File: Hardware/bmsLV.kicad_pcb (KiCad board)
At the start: 2 copper layers, 45 parts, among them J1 Conn_01x06_Male, J2 Conn_01x03_Female, J3 Conn_01x03_Female, J4 Conn_01x02_Female, J5 Conn_01x02_Female, SW1 SW_Push, U1 STM32F103C8Tx, U2 LM1117-3.3, U3 LM1117-3.3, U4 LM1117-3.3, U5 LM2596S-5, U6 MCP2562-H-SN, Y1 Crystal

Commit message: Going back to work
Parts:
- removed U5: LM2596S-5, Package_TO_SOT_SMD:TO-263-5_TabPin3
- removed U6: MCP2562-H-SN, Package_SO:SOIC-8_3.9x4.9mm_P1.27mm
- added C20: 10nF, Capacitor_SMD:C_1206_3216Metric, F.Cu at (210.8, 58.6)
- added C21: 10nF, Capacitor_SMD:C_1206_3216Metric, F.Cu at (173.5, 85.5)
- added C22: 10nF, Capacitor_SMD:C_1206_3216Metric, F.Cu at (202.5, 67.4)
- added C23: 10nF, Capacitor_SMD:C_1206_3216Metric, F.Cu at (217.2, 53.0)
- added C24: 10nF, Capacitor_SMD:C_1206_3216Metric, F.Cu at (185.0, 82.2)
- added C25: 1u, Capacitor_SMD:C_1206_3216Metric, F.Cu at (202.5, 64.1)
- added C26: 1u, Capacitor_SMD:C_1206_3216Metric, F.Cu at (179.1, 85.5)
- added C27: 1u, Capacitor_SMD:C_1206_3216Metric, F.Cu at (184.7, 85.5)
- added C28: 1u, Capacitor_SMD:C_1206_3216Metric, F.Cu at (179.4, 82.2)
- added C29: 0.1u, Capacitor_SMD:C_0603_1608Metric, F.Cu at (195.1, 87.2)
- added C30: 100n, Capacitor_SMD:C_1206_3216Metric, F.Cu at (253.8, 99.9)
- added C31: 100n, Capacitor_SMD:C_1206_3216Metric, F.Cu at (253.8, 96.6)
- added C32: 100n, Capacitor_SMD:C_1206_3216Metric, F.Cu at (236.0, 111.4)
- added C33: 100n, Capacitor_SMD:C_1206_3216Metric, F.Cu at (253.8, 93.3)
- added C34: 100n, Capacitor_SMD:C_1206_3216Metric, F.Cu at (230.4, 111.4)
- added C35: 100n, Capacitor_SMD:C_1206_3216Metric, F.Cu at (219.1, 111.4)
- added D10: 9.1V, Diode_SMD:D_SMB, F.Cu at (189.1, 72.2)
- added D11: 9.1V, Diode_SMD:D_SMB, F.Cu at (201.9, 54.1)
- added D12: 9.1V, Diode_SMD:D_SMB, F.Cu at (180.8, 77.8)
- added D13: 9.1V, Diode_SMD:D_SMB, F.Cu at (189.1, 77.8)
- added D14: 9.1V, Diode_SMD:D_SMB, F.Cu at (180.8, 72.2)
- added D15: 9.1V, Diode_SMD:D_SMB, F.Cu at (210.2, 54.1)
- added D16: D_Small, Diode_SMD:D_SMB, F.Cu at (130.4, 69.8)
- added D5: D_Schottky, Diode_SMD:D_SMB, F.Cu at (36.4, 109.9)
- added D6: D_Schottky, Diode_SMD:D_SMB, F.Cu at (78.3, 106.0)
- added D7: D_Schottky, Diode_SMD:D_SMB, F.Cu at (44.2, 114.9)
- added D8: D_TVS_x2_AAC, Package_TO_SOT_SMD:SOT-23, F.Cu at (159.3, 118.7)
- added D9: 9.1V, Diode_SMD:D_SMB, F.Cu at (203.9, 59.7)
- added FB1: Ferrite_Bead_Small, Capacitor_SMD:C_1206_3216Metric, F.Cu at (36.7, 106.0)
- added J10: Conn_01x01_Female, Connector_Pin:Pin_D1.0mm_L10.0mm_LooseFit, F.Cu at (48.2, 62.2)
- added J11: Conn_01x01_Female, Connector_Pin:Pin_D1.0mm_L10.0mm_LooseFit, F.Cu at (27.9, 62.2)
- added J12: Conn_01x01_Female, Connector_Pin:Pin_D1.0mm_L10.0mm_LooseFit, F.Cu at (28.1, 112.7)
- added J13: Conn_01x04_Male, Connector_PinHeader_2.54mm:PinHeader_1x04_P2.54mm_Vertical, F.Cu at (122.6, 109.9)
- added J6: Conn_01x01_Female, Connector_Pin:Pin_D1.0mm_L10.0mm_LooseFit, F.Cu at (129.1, 62.2)
- added J7: Conn_01x01_Female, Connector_Pin:Pin_D1.0mm_L10.0mm_LooseFit, F.Cu at (108.9, 62.2)
- added J8: Conn_01x01_Female, Connector_Pin:Pin_D1.0mm_L10.0mm_LooseFit, F.Cu at (88.7, 62.2)
- added J9: Conn_01x01_Female, Connector_Pin:Pin_D1.0mm_L10.0mm_LooseFit, F.Cu at (68.4, 62.2)
- added K1: RM85V7, RM85V7:RM85V7, F.Cu at (130.2, 92.7)
- added LTC1: LTC6810-1, Package_SO:SSOP-44_5.3x12.8mm_P0.5mm, F.Cu at (171.2, 58.5)
- added Q1: BSS138, Package_TO_SOT_SMD:SOT-23, F.Cu at (124.2, 69.5)
- added Q2: Q_PMOS_GSD, Package_TO_SOT_SMD:SOT-23W, F.Cu at (212.6, 72.3)
- added Q3: Q_PMOS_GSD, Package_TO_SOT_SMD:SOT-23W, F.Cu at (219.0, 63.5)
- added Q4: Q_PMOS_GSD, Package_TO_SOT_SMD:SOT-23W, F.Cu at (228.1, 56.9)
- added Q5: Q_PMOS_GSD, Package_TO_SOT_SMD:SOT-23W, F.Cu at (201.5, 84.9)
- added Q6: Q_PMOS_GSD, Package_TO_SOT_SMD:SOT-23W, F.Cu at (223.9, 63.5)
- added Q7: Q_PMOS_GSD, Package_TO_SOT_SMD:SOT-23W, F.Cu at (207.1, 78.9)
- added Q8: Q_PMOS_GSD, Package_TO_SOT_SMD:SOT-23W, F.Cu at (212.6, 76.9)
- added Q9: Q_NPN_BCE, Package_TO_SOT_SMD:SOT-23W, F.Cu at (219.0, 68.0)
- added R10: 30, Resistor_SMD:R_1206_3216Metric, F.Cu at (228.4, 53.0)
- added R11: 30, Resistor_SMD:R_1206_3216Metric, F.Cu at (196.1, 71.1)
- added R12: 30, Resistor_SMD:R_1206_3216Metric, F.Cu at (167.8, 85.5)
- added R13: 30, Resistor_SMD:R_1206_3216Metric, F.Cu at (201.7, 71.1)
- added R14: 30, Resistor_SMD:R_1206_3216Metric, F.Cu at (207.3, 75.0)
- added R15: 30, Resistor_SMD:R_1206_3216Metric, F.Cu at (201.8, 81.0)
- added R16: 30, Resistor_SMD:R_1206_3216Metric, F.Cu at (213.7, 68.4)
- added R17: 1k, Resistor_SMD:R_1206_3216Metric, F.Cu at (222.1, 59.6)
- added R18: 1k, Resistor_SMD:R_1206_3216Metric, F.Cu at (201.7, 77.7)
- added R19: 1k, Resistor_SMD:R_1206_3216Metric, F.Cu at (207.3, 71.7)
- added R20: 1k, Resistor_SMD:R_1206_3216Metric, F.Cu at (196.2, 84.3)
- added R21: 1k, Resistor_SMD:R_1206_3216Metric, F.Cu at (190.6, 82.2)
- added R22: 1k, Resistor_SMD:R_1206_3216Metric, F.Cu at (213.7, 65.1)
- added R23: 1k, Resistor_SMD:R_1206_3216Metric, F.Cu at (222.8, 56.3)
- added R24: 100, Resistor_SMD:R_1206_3216Metric, F.Cu at (196.2, 81.0)
- added R25: 100, Resistor_SMD:R_1206_3216Metric, F.Cu at (208.1, 68.4)
- added R26: 100, Resistor_SMD:R_1206_3216Metric, F.Cu at (216.5, 59.6)
- added R27: 100, Resistor_SMD:R_1206_3216Metric, F.Cu at (201.7, 74.4)
- added R28: 100, Resistor_SMD:R_1206_3216Metric, F.Cu at (208.1, 65.1)
- added R29: 100, Resistor_SMD:R_1206_3216Metric, F.Cu at (190.3, 85.5)
- added R30: 100, Resistor_SMD:R_1206_3216Metric, F.Cu at (196.1, 77.7)
- added R31: 100, Resistor_SMD:R_1206_3216Metric, F.Cu at (222.8, 53.0)
- added R32: 100, Resistor_SMD:R_1206_3216Metric, F.Cu at (217.2, 56.3)
- added R33: 10K, Resistor_SMD:R_1206_3216Metric, F.Cu at (224.7, 111.4)
- added R34: 10K, Resistor_SMD:R_1206_3216Metric, F.Cu at (241.6, 111.4)
- added R35: 10K, Resistor_SMD:R_1206_3216Metric, F.Cu at (253.8, 103.2)
- added R36: 10K, Resistor_SMD:R_1206_3216Metric, F.Cu at (247.2, 111.4)
- added R37: 10K, Resistor_SMD:R_1206_3216Metric, F.Cu at (253.8, 106.5)
- added R38: 10K, Resistor_SMD:R_1206_3216Metric, F.Cu at (252.8, 111.4)
- added R39: 27, Resistor_SMD:R_1206_3216Metric, F.Cu at (153.3, 87.9)
- added R40: 27, Resistor_SMD:R_1206_3216Metric, F.Cu at (153.3, 91.2)
- added R7: 100, Resistor_SMD:R_1206_3216Metric, F.Cu at (118.7, 70.0)
- added R8: 10K, Resistor_SMD:R_1206_3216Metric, F.Cu at (121.3, 70.0)
- added R9: 120, Resistor_SMD:R_1206_3216Metric, F.Cu at (170.2, 114.9)
- added TH1: Thermistor_PTC, TerminalBlock:TerminalBlock_bornier-2_P5.08mm, F.Cu at (242.7, 105.2)
- added TH2: Thermistor_PTC, TerminalBlock:TerminalBlock_bornier-2_P5.08mm, F.Cu at (242.7, 96.2)
- added TH3: Thermistor_PTC, TerminalBlock:TerminalBlock_bornier-2_P5.08mm, F.Cu at (231.1, 105.2)
- added TH4: Thermistor_PTC, TerminalBlock:TerminalBlock_bornier-2_P5.08mm, F.Cu at (231.1, 96.2)
- added TH5: Thermistor_PTC, TerminalBlock:TerminalBlock_bornier-2_P5.08mm, F.Cu at (219.6, 105.2)
- added TH6: Thermistor_PTC, TerminalBlock:TerminalBlock_bornier-2_P5.08mm, F.Cu at (219.6, 96.2)
- C1, C2: value C_Small -> 22p
- C10: value CP_Small -> 47n; footprint Capacitor_SMD:CP_Elec_6.3x7.7 -> Capacitor_SMD:C_1206_3216Metric
- C11: value C_Small -> 680u; footprint Capacitor_SMD:C_1206_3216Metric -> Capacitor_SMD:CP_Elec_6.3x7.7
- C12, C13, C14, C16, C3, C4, C5, C6, C7, C8: value C_Small -> 100n
- C15: value C_Small -> 220uF; footprint Capacitor_SMD:C_1206_3216Metric -> Capacitor_SMD:CP_Elec_6.3x7.7
- C17: value CP_Small -> 100n; footprint Capacitor_SMD:CP_Elec_6.3x7.7 -> Capacitor_SMD:C_1206_3216Metric
- C18, C19: value C_Small -> 10nF
- C9: value C_Small -> 330p
- D2, D3: value D_Schottky -> LED; footprint Diode_SMD:D_SMB -> LED_SMD:LED_1206_3216Metric
- D4: value D_TVS_x2_AAC -> LED; footprint Package_TO_SOT_SMD:SOT-23 -> LED_SMD:LED_1206_3216Metric
- J2: value Conn_01x03_Female -> USB_B_Mini; footprint TerminalBlock:TerminalBlock_bornier-3_P5.08mm -> Connector_USB:USB_Micro-B_Molex_47346-0001
- J3: value Conn_01x03_Female -> Conn_01x02_Female; footprint TerminalBlock:TerminalBlock_bornier-3_P5.08mm -> TerminalBlock:TerminalBlock_bornier-2_P5.08mm
- J4: value Conn_01x02_Female -> Conn_01x02_Male; footprint TerminalBlock:TerminalBlock_bornier-2_P5.08mm -> Connector_PinHeader_2.54mm:PinHeader_1x02_P2.54mm_Vertical
- L1: value L_Small -> 10u
- L2: value L_Small -> 33u
- R1, R2: value 100K -> 120
- R3: value 500 -> 120
- R4: value R_Small -> 120
- R5: value R_Small -> 100K
- R6: value 120 -> 100K
- U3: value LM1117-3.3 -> LM2596S-5; footprint Package_TO_SOT_SMD:SOT-223 -> Package_TO_SOT_SMD:TO-263-5_TabPin3
- U4: value LM1117-3.3 -> MCP2562-H-SN; footprint Package_TO_SOT_SMD:SOT-223 -> Package_SO:SOIC-8_3.9x4.9mm_P1.27mm
- moved C18 124.8 mm to (210.8, 61.8)
- moved J3 115.7 mm to (33.0, 96.5), turned to 270 degrees
- moved C19 100.6 mm to (196.1, 74.4)
- moved F1 95.3 mm to (36.4, 114.9), turned to 180 degrees
- moved C16 91.1 mm to (177.2, 125.9), turned to 270 degrees
- moved SW1 90.3 mm to (93.3, 110.4)
- moved C6 88.7 mm to (100.2, 105.4), turned to 180 degrees
- moved L1 87.8 mm to (100.3, 108.0)
- moved C9 86.9 mm to (43.2, 106.0), turned to 180 degrees
- moved C12 83.4 mm to (43.0, 111.1), turned to 180 degrees
- moved Y1 81.2 mm to (94.6, 99.5), turned to 270 degrees
- moved J5 79.5 mm to (160.0, 128.9)
- moved U4 79.4 mm to (174.7, 120.7)
- moved R4 78.3 mm to (111.1, 114.4), turned to 270 degrees
- moved C1 77.7 mm to (99.1, 97.0), turned to 270 degrees
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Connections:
- C11 pad 1: +5V -> Net-(C10-Pad1)
- C12 pad 1: +5V -> Net-(C10-Pad1)
- C15 pad 1: +3.3VA -> +5VD
- C16 pad 1: +3.3VADC -> SW_VDD
- C18 pad 1: SW_VDD -> SW_GND
- C18 pad 2: SW_GND -> Net-(C18-Pad2)
- C19 pad 1: +5V -> SW_GND
- C19 pad 2: SW_GND -> Net-(C19-Pad2)
- C9 pad 1: Net-(C10-Pad1) -> Net-(C9-Pad1)
- D2 pad 1: Net-(C10-Pad1) -> Net-(D2-Pad1)
- D2 pad 2: SW_GND -> Net-(D2-Pad2)
- D3 pad 2: SW_GND -> Net-(D3-Pad2)
- D4 pad 1: CANL -> Net-(D4-Pad1)
- D4 pad 2: CANH -> Net-(D4-Pad2)
- F1 pad 1: Net-(C10-Pad1) -> Net-(C9-Pad1)
- F1 pad 2: Net-(F1-Pad2) -> VCC
- J2 pad 1: Net-(J2-Pad1) -> +5V
- J2 pad 2: Ain0 -> USB_DM
- J2 pad 3: SW_GND -> USB_DP
- J3 pad 1: +3.3VADC -> SW_GND
- J3 pad 2: Ain1 -> VCC
- J4 pad 1: SW_GND -> CANL
- J4 pad 2: Net-(F1-Pad2) -> Net-(J4-Pad2)
- L2 pad 1: Net-(D3-Pad1) -> Net-(D7-Pad1)
- L2 pad 2: +5V -> +5VD
- R1 pad 1: SW_VDD -> Net-(D1-Pad2)
- R1 pad 2: SW_NRST -> SW_VDD
- R2 pad 1: Net-(R2-Pad1) -> Net-(D2-Pad2)
- R2 pad 2: SW_GND -> SW_VDD
- R3 pad 1: SW_VDD -> Net-(D3-Pad2)
- R3 pad 2: Net-(D1-Pad2) -> SW_VDD
- R4 pad 1: +3.3VA -> Net-(D4-Pad2)
- R4 pad 2: Net-(J2-Pad1) -> SW_VDD
- R5 pad 1: Net-(J3-Pad3) -> SW_VDD
- R5 pad 2: SW_GND -> SW_NRST
- R6 pad 1: CANH -> Net-(R6-Pad1)
- R6 pad 2: CANL -> SW_GND
- U1 pad 10: Ain0 -> Net-(U1-Pad10)
- U1 pad 11: Ain1 -> Net-(U1-Pad11)
- U1 pad 12: Net-(U1-Pad12) -> En_Relay
- U1 pad 13: Net-(U1-Pad13) -> Term_1
- U1 pad 14: Net-(U1-Pad14) -> Term_2
- U1 pad 15: Net-(D1-Pad1) -> Term_3
- U1 pad 16: Net-(U1-Pad16) -> Term_4
- U1 pad 17: Net-(U1-Pad17) -> Term_5
- U1 pad 18: Net-(U1-Pad18) -> Term_6
- U1 pad 19: Net-(U1-Pad19) -> Net-(D1-Pad1)
- U1 pad 20: Net-(U1-Pad20) -> Net-(D2-Pad1)
- U1 pad 21: Net-(U1-Pad21) -> Net-(D3-Pad1)
- U1 pad 22: Net-(U1-Pad22) -> Net-(D4-Pad1)
- U1 pad 32: RX_Can -> Net-(R39-Pad2)
- U1 pad 33: TX_Can -> Net-(R40-Pad2)
- U1 pad 38: Net-(U1-Pad38) -> CS
- U1 pad 39: Net-(U1-Pad39) -> SCK
- U1 pad 40: Net-(U1-Pad40) -> MISO
- U1 pad 41: Net-(U1-Pad41) -> MOSI
- U1 pad 44: Net-(R2-Pad1) -> Net-(R6-Pad1)
- U1 pad 45: Net-(U1-Pad45) -> RX_Can
- U1 pad 46: Net-(U1-Pad46) -> TX_Can
- U3 pad 1: SW_GND -> Net-(C10-Pad1)
- U3 pad 2: +3.3VA -> Net-(D7-Pad1)
- U3 pad 3: +5V -> SW_GND
- U3 pad 4: (no net) -> +5VD
- U4 pad 1: SW_GND -> TX_Can
- U4 pad 2: +3.3VADC -> SW_GND
- U4 pad 4: (no net) -> RX_Can
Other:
- board outline added: 121.2 x 60.6 mm

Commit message: pcb layout nearly done
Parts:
- added D17: LED_Small, LED_SMD:LED_0805_2012Metric, F.Cu at (146.1, 64.8)
- added D18: LED_Small, LED_SMD:LED_0805_2012Metric, F.Cu at (123.2, 65.2)
- added D19: LED_Small, LED_SMD:LED_0805_2012Metric, F.Cu at (102.9, 65.2)
- added D20: LED_Small, LED_SMD:LED_0805_2012Metric, F.Cu at (83.2, 65.2)
- added D21: LED_Small, LED_SMD:LED_0805_2012Metric, F.Cu at (62.9, 65.2)
- added D22: LED_Small, LED_SMD:LED_0805_2012Metric, F.Cu at (42.5, 65.2)
- added D23: LED_Small, LED_SMD:LED_0805_2012Metric, F.Cu at (25.9, 68.7)
- added R41: 330, Resistor_SMD:R_1206_3216Metric, F.Cu at (146.1, 60.5)
- added R42: 330, Resistor_SMD:R_1206_3216Metric, F.Cu at (123.2, 61.1)
- added R43: 330, Resistor_SMD:R_1206_3216Metric, F.Cu at (102.9, 61.1)
- added R44: 330, Resistor_SMD:R_1206_3216Metric, F.Cu at (83.2, 61.1)
- added R45: 330, Resistor_SMD:R_1206_3216Metric, F.Cu at (62.9, 61.1)
- added R46: 330, Resistor_SMD:R_1206_3216Metric, F.Cu at (42.5, 61.1)
- added R47: 330, Resistor_SMD:R_1206_3216Metric, F.Cu at (21.7, 68.7)
- J10, J11, J12, J6, J7, J8, J9: footprint Connector_Pin:Pin_D1.0mm_L10.0mm_LooseFit -> CellPad:CellPad
- R10, R11, R12, R13, R14, R15, R16: footprint Resistor_SMD:R_1206_3216Metric -> Resistor_SMD:R_2512_6332Metric
- TH1, TH2, TH3, TH4, TH5, TH6: footprint TerminalBlock:TerminalBlock_bornier-2_P5.08mm -> Connector_PinHeader_2.54mm:PinHeader_1x02_P2.54mm_Vertical
- moved C30 233.1 mm to (20.7, 102.5), turned to 180 degrees
- moved C31 233.1 mm to (20.7, 99.1), turned to 180 degrees
- moved C33 233.1 mm to (20.7, 92.1), turned to 180 degrees
- moved R35 222.4 mm to (31.6, 92.2)
- moved R37 222.3 mm to (31.6, 99.1)
- moved R38 221.4 mm to (31.6, 102.5)
- moved TH1 218.7 mm to (24.9, 85.3), turned to 90 degrees
- moved TH2 217.9 mm to (24.9, 88.8), turned to 90 degrees
- moved R36 216.1 mm to (31.6, 95.6)
- moved C32 215.8 mm to (20.7, 95.6), turned to 180 degrees
- moved R34 211.2 mm to (31.6, 88.8)
- moved C34 210.9 mm to (20.7, 88.8), turned to 180 degrees
- moved TH3 206.6 mm to (24.9, 92.2), turned to 90 degrees
- moved TH4 206.2 mm to (24.9, 95.6), turned to 90 degrees
- moved C35 200.1 mm to (20.7, 85.3), turned to 180 degrees
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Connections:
- D14 pad 2: SW_GND -> Net-(BT5-Pad2)
- J11 pad 1: SW_GND -> Net-(BT5-Pad2)
- Q7 pad 2: SW_GND -> Net-(BT5-Pad2)
- R16 pad 1: SW_GND -> Net-(BT5-Pad2)
- R22 pad 2: SW_GND -> Net-(BT5-Pad2)
- R28 pad 1: SW_GND -> Net-(BT5-Pad2)
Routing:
- net Term_5: track 0.00 -> 0.72 mm
- net SW_GND: vias 0 -> 35
- added copper zone on F.Cu, net SW_GND

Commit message: PCB layout v1
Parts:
- added R48: 10k, Resistor_SMD:R_0805_2012Metric, F.Cu at (84.6, 91.9)
- added R49: 10k, Resistor_SMD:R_0805_2012Metric, F.Cu at (82.7, 91.9)
- added R50: 10k, Resistor_SMD:R_0805_2012Metric, F.Cu at (80.8, 91.9)
- added R51: 10k, Resistor_SMD:R_0805_2012Metric, F.Cu at (78.9, 91.9)
- moved C23 202.7 mm to (22.6, 109.9), turned to 90 degrees
- moved R23 192.7 mm to (31.5, 79.1), turned to 270 degrees
- moved Q8 185.0 mm to (27.6, 81.3), turned to 180 degrees
- moved D15 177.0 mm to (35.1, 79.9), turned to 270 degrees
- moved R22 176.2 mm to (37.6, 70.6), turned to 270 degrees
- moved R29 171.7 mm to (20.3, 109.9), turned to 90 degrees
- moved R28 167.0 mm to (41.3, 73.2)
- moved Q7 166.4 mm to (41.0, 70.1)
- moved Q6 163.1 mm to (61.0, 70.1)
- moved C22 161.4 mm to (41.3, 75.4)
- moved D14 146.7 mm to (34.0, 72.0), turned to 270 degrees
- moved R27 140.4 mm to (61.3, 73.2)
- moved R26 135.9 mm to (81.3, 73.2)
- moved D13 135.1 mm to (54.1, 72.0), turned to 270 degrees
- moved R21 133.5 mm to (57.7, 70.6), turned to 270 degrees
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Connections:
- LTC1 pad 34: SW_GND -> Net-(LTC1-Pad34)
- LTC1 pad 35: SW_GND -> Net-(LTC1-Pad35)
- LTC1 pad 38: SW_GND -> Net-(LTC1-Pad38)
- LTC1 pad 39: SW_GND -> Net-(LTC1-Pad39)
- R32 pad 1: Net-(BT1-Pad1) -> Net-(R32-Pad1)
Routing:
- added copper zone on F.Cu, net Net-(BT1-Pad1)
- added copper zone on F.Cu, net Net-(BT1-Pad2)
- added copper zone on F.Cu, net Net-(BT2-Pad2)
- added copper zone on F.Cu, net Net-(BT3-Pad2)
- added copper zone on F.Cu, net Net-(BT4-Pad2)
- added copper zone on F.Cu, net Net-(BT5-Pad2)
- added copper zone on F.Cu, net Net-(D18-Pad1)
- added copper zone on F.Cu, net Net-(D19-Pad1)
- added copper zone on F.Cu, net Net-(D20-Pad1)
- added copper zone on F.Cu, net Net-(D21-Pad1)
- added copper zone on F.Cu, net Net-(D22-Pad1)
- added copper zone on F.Cu, net Net-(D23-Pad1)

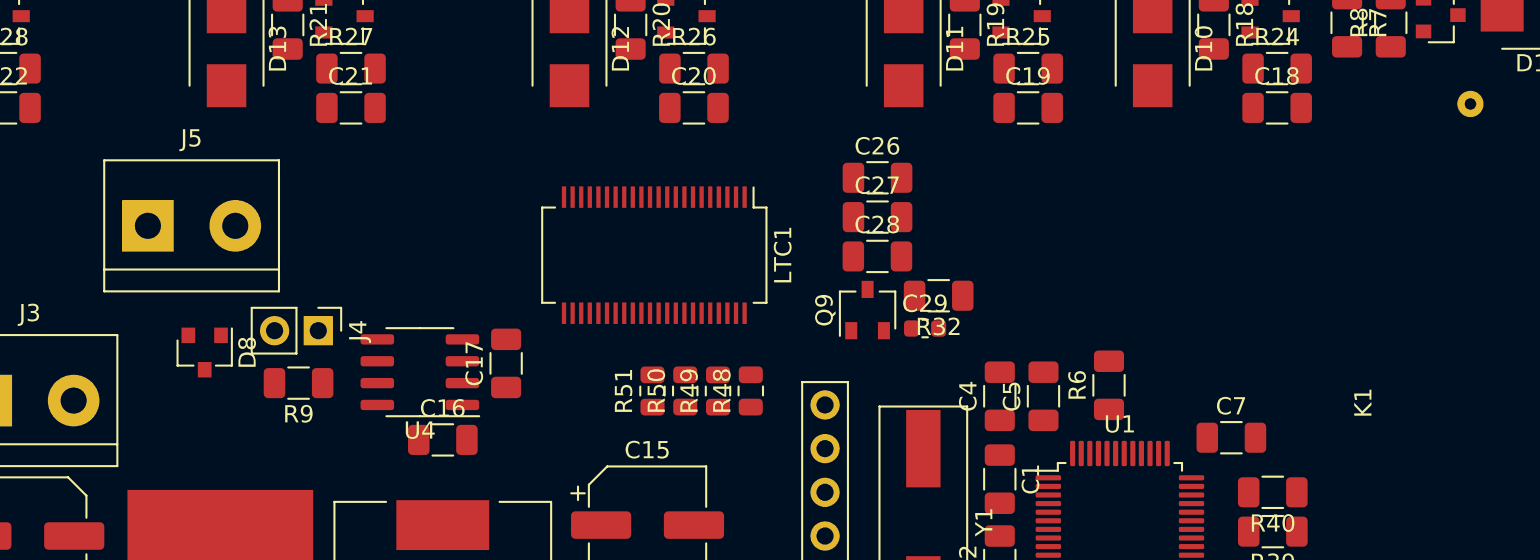
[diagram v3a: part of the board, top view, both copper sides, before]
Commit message: PCB v2
changes in scheme:
NMOS->PMOS in LTC balance
S6 LTC pinout deleted
another discharge resistor added on every S# LTC pinout and value changed from 30 to 68 on both
PCB changes:
CAN position changed
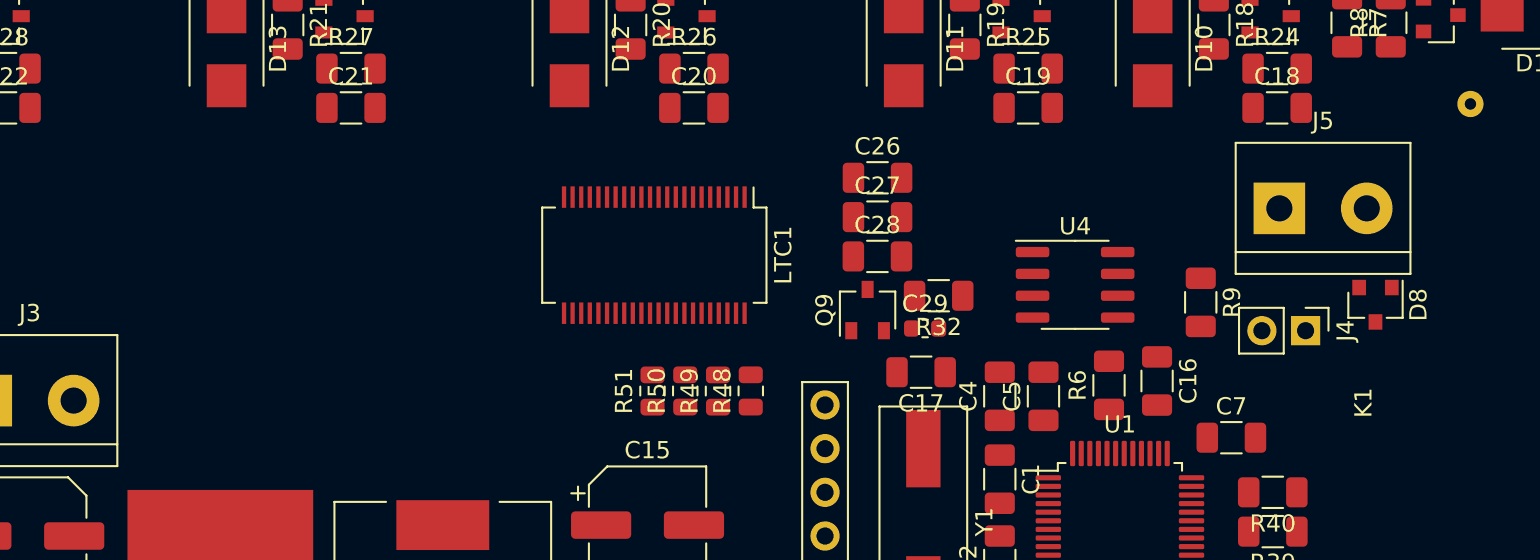
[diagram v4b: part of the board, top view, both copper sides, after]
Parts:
- moved D8 68.1 mm to (120.9, 86.9)
- moved J5 65.8 mm to (115.3, 81.3)
- moved J4 57.4 mm to (116.8, 88.4)
- moved R9 52.7 mm to (110.7, 86.7), turned to 270 degrees
- moved C16 41.7 mm to (108.2, 91.3), turned to 270 degrees
- moved U4 38.4 mm to (103.4, 85.7), turned to 0 degrees
- moved C17 24.1 mm to (94.5, 90.8), turned to 180 degrees

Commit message: PCB finished
PCB finished and ready to check
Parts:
- removed D17: LED_Small, LED_SMD:LED_0805_2012Metric
- removed D9: 9.1V, Diode_SMD:D_SMB
- removed Q8: Q_PMOS_GSD, Package_TO_SOT_SMD:SOT-23W
- removed R10: 30, Resistor_SMD:R_2512_6332Metric
- removed R17: 1k, Resistor_SMD:R_1206_3216Metric
- removed R41: 330, Resistor_SMD:R_1206_3216Metric
- added J14: Conn_01x02_Male, Connector_PinHeader_2.54mm:PinHeader_1x02_P2.54mm_Vertical, F.Cu at (101.1, 81.3)
- added J15: Conn_01x02_Male, Connector_PinHeader_2.54mm:PinHeader_1x02_P2.54mm_Vertical, F.Cu at (94.7, 81.3)
- added J16: Conn_01x02_Male, Connector_PinHeader_2.54mm:PinHeader_1x02_P2.54mm_Vertical, F.Cu at (88.4, 81.3)
- added R53: 68, Resistor_SMD:R_2512_6332Metric, F.Cu at (116.3, 63.1)
- added R54: 68, Resistor_SMD:R_2512_6332Metric, F.Cu at (96.0, 63.2)
- added R55: 68, Resistor_SMD:R_2512_6332Metric, F.Cu at (75.8, 63.1)
- added R56: 68, Resistor_SMD:R_2512_6332Metric, F.Cu at (55.6, 63.1)
- added R57: 68, Resistor_SMD:R_2512_6332Metric, F.Cu at (35.4, 63.0)
- added R58: 68, Resistor_SMD:R_2512_6332Metric, F.Cu at (23.7, 78.4)
- Q2, Q3, Q4, Q5, Q6, Q7: value Q_PMOS_GSD -> Q_NMOS_GSD; footprint Package_TO_SOT_SMD:SOT-23W -> Package_TO_SOT_SMD:SOT-23
- R11, R12, R13, R14, R15, R16: value 30 -> 68
- moved C24 75.5 mm to (88.9, 84.3)
- moved R30 71.7 mm to (93.5, 84.3), turned to 180 degrees
- moved C25 70.2 mm to (87.8, 87.8), turned to 270 degrees
- moved R31 66.9 mm to (91.3, 86.6)
- moved C23 50.6 mm to (66.0, 84.0)
- moved R29 50.6 mm to (63.8, 84.0)
- moved Q2 47.4 mm to (115.3, 70.1)
- moved C26 27.3 mm to (67.8, 92.2), turned to 270 degrees
- moved C27 24.2 mm to (70.1, 92.2), turned to 270 degrees
- moved C28 21.2 mm to (72.4, 92.2), turned to 270 degrees
- moved C29 19.6 mm to (76.2, 94.7), turned to 180 degrees
- moved Q6 19.4 mm to (41.5, 70.1)
- moved Q5 19.0 mm to (61.9, 70.1)
- moved Q4 18.1 mm to (82.2, 70.1)
- moved R32 17.5 mm to (80.1, 94.7)
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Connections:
- LTC1 pad 28: Net-(LTC1-Pad28) -> SW_GND
- LTC1 pad 40: MOSI -> MISO
- LTC1 pad 41: MISO -> MOSI
- LTC1 pad 5: Net-(D9-Pad1) -> Net-(J14-Pad1)
- Q2 pad 1: Net-(D9-Pad1) -> Net-(D10-Pad1)
- Q2 pad 2: Net-(BT1-Pad1) -> Net-(BT1-Pad2)
- Q2 pad 3: Net-(D17-Pad1) -> Net-(D18-Pad1)
- Q3 pad 1: Net-(D10-Pad1) -> Net-(D11-Pad1)
- Q3 pad 2: Net-(BT1-Pad2) -> Net-(BT2-Pad2)
- Q3 pad 3: Net-(D18-Pad1) -> Net-(D19-Pad1)
- Q4 pad 1: Net-(D11-Pad1) -> Net-(D12-Pad1)
- Q4 pad 2: Net-(BT2-Pad2) -> Net-(BT3-Pad2)
- Q4 pad 3: Net-(D19-Pad1) -> Net-(D20-Pad1)
- Q5 pad 1: Net-(D12-Pad1) -> Net-(D13-Pad1)
- Q5 pad 2: Net-(BT3-Pad2) -> Net-(BT4-Pad2)
- Q5 pad 3: Net-(D20-Pad1) -> Net-(D21-Pad1)
- Q6 pad 1: Net-(D13-Pad1) -> Net-(D14-Pad1)
- Q6 pad 2: Net-(BT4-Pad2) -> Net-(BT5-Pad2)
- Q6 pad 3: Net-(D21-Pad1) -> Net-(D22-Pad1)
- Q7 pad 1: Net-(D14-Pad1) -> Net-(D15-Pad1)
- Q7 pad 2: Net-(BT5-Pad2) -> SW_GND
- Q7 pad 3: Net-(D22-Pad1) -> Net-(D23-Pad1)
- R32 pad 1: Net-(R32-Pad1) -> Net-(BT1-Pad1)
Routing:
- net SW_VDD: track 0.00 -> 212.8 mm, vias 0 -> 6
- net Term_6: track 0.00 -> 113.4 mm, vias 0 -> 1
- net Term_4: track 0.00 -> 111.0 mm, vias 0 -> 1
- net Term_3: track 0.00 -> 110.9 mm, vias 0 -> 1
- net Term_5: track 0.72 -> 110.3 mm, vias 0 -> 1
- net Term_2: track 0.00 -> 106.4 mm, vias 0 -> 1
- net Term_1: track 0.00 -> 101.5 mm, vias 0 -> 1
- net En_Relay: track 0.00 -> 100.8 mm, vias 0 -> 2
- net Net-(BT1-Pad1): track 0.00 -> 99.4 mm, vias 0 -> 6
- net +5V: track 0.00 -> 91.2 mm, vias 0 -> 1
- net SW_GND: track 0.00 -> 71.9 mm, vias 35 -> 49
- net Net-(D14-Pad1): track 0.00 -> 62.8 mm, vias 0 -> 2
- net Net-(BT5-Pad2): track 0.00 -> 50.5 mm
- net SW_NRST: track 0.00 -> 48.8 mm
- net Net-(D10-Pad1): track 0.00 -> 48.8 mm, vias 0 -> 2
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- added copper zone on B.Cu, net SW_GND
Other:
- outline, holes or cut-outs redrawn
